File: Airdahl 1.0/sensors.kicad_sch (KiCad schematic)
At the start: 26 parts, among them J7 CONUFL001-SMD-T, J9 104031-0811, U4 BNO085, U5 BMP581, U6 RFM95W-915S2

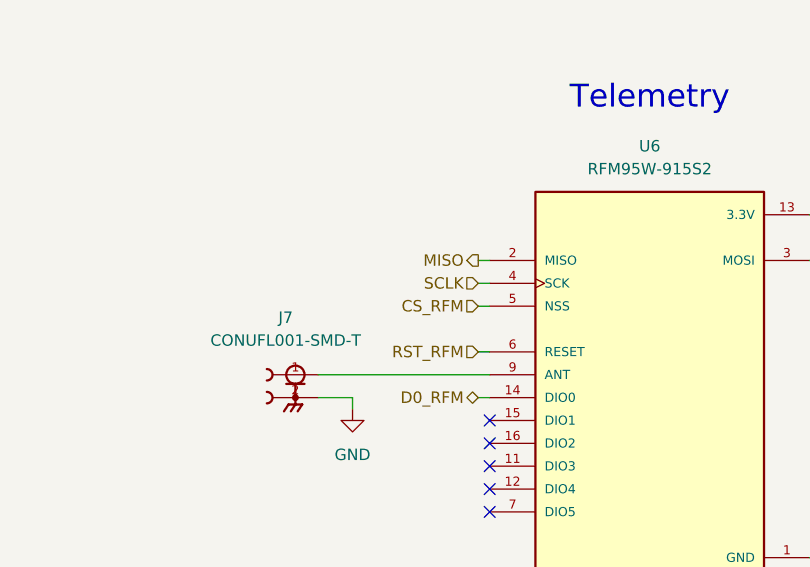
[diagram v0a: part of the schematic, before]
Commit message: H-Bridge wiring + motor ports, cleaned up carrier schematics, added MISO source terminating resistors on carriers
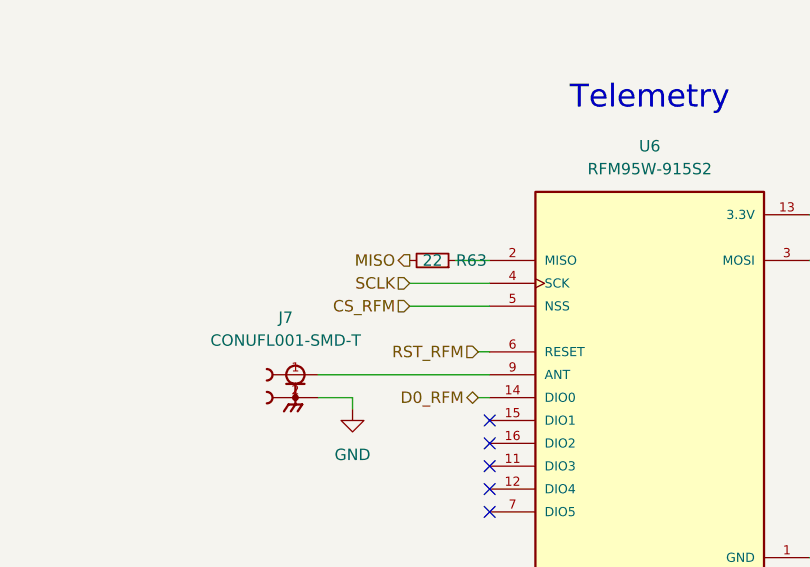
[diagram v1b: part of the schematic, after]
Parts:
- added R63: 22, Resistor_SMD:R_0402_1005Metric, symbol Device:R_Small
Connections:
- net MISO: now also R63.2; no longer U6.2 (MISO)
- new net: R63.1, U6.2 (MISO)
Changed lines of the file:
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@@
 	(wire
 		(pts
-			(xy 218.44 102.87) (xy 219.71 102.87)
+			(xy 210.82 102.87) (xy 219.71 102.87)
 		)
 		(stroke
@@
 	(wire
 		(pts
-			(xy 218.44 100.33) (xy 219.71 100.33)
+			(xy 210.82 100.33) (xy 219.71 100.33)
 		)
 		(stroke
@@
 	(wire
 		(pts
-			(xy 218.44 97.79) (xy 219.71 97.79)
-		)
-		(stroke
-			(width 0)
-			(type default)
-		)
-	)
-	(wire
-		(pts
 			(xy 52.07 146.05) (xy 48.26 146.05)
 		)
@@
 	(wire
 		(pts
+			(xy 215.9 97.79) (xy 219.71 97.79)
+		)
+		(stroke
+			(width 0)
+			(type default)
+		)
+	)
+	(wire
+		(pts
 			(xy 96.52 48.26) (xy 111.76 48.26)
 		)
@@
 	(hierarchical_label "SCLK"
 		(shape input)
-		(at 218.44 100.33 180)
+		(at 210.82 100.33 180)
 		(effects
 			(font
@@
 	(hierarchical_label "MISO"
 		(shape output)
-		(at 218.44 97.79 180)
+		(at 210.82 97.79 180)
 		(effects
 			(font
@@
 	(hierarchical_label "CS_RFM"
 		(shape input)
-		(at 218.44 102.87 180)
+		(at 210.82 102.87 180)
 		(effects
 			(font
@@
 					(unit 1)
 				)
+			)
+		)
+	)
+	(symbol
+		(lib_id "Device:R_Small")
+		(at 213.36 97.79 270)
+		(mirror x)
+		(unit 1)
+		(body_style 1)
+		(exclude_from_sim no)
+		(in_bom yes)
+		(on_board yes)
+		(in_pos_files yes)
+		(dnp no)
+		(property "Reference" "R63"
+			(at 217.678 97.79 90)
+			(show_name no)
+			(do_not_autoplace no)
+			(effects
+				(font
+					(size 1.27 1.27)
+				)
+			)
+		)
+		(property "Value" "22"
+			(at 213.36 97.79 90)
+			(show_name no)
+			(do_not_autoplace no)
+			(effects
+				(font
+					(size 1.27 1.27)
+				)
+			)
+		)
+		(property "Footprint" "Resistor_SMD:R_0402_1005Metric"
+			(at 213.36 97.79 0)
+			(hide yes)
+			(show_name no)
+			(do_not_autoplace no)
+			(effects
+				(font
+					(size 1.27 1.27)
+				)
+			)
+		)
+		(property "Datasheet" ""
+			(at 213.36 97.79 0)
+			(hide yes)
+			(show_name no)
+			(do_not_autoplace no)
+			(effects
+				(font
+					(size 1.27 1.27)
+				)
+			)
+		)
+		(property "Description" "Resistor, small symbol"
+			(at 213.36 97.79 0)
+			(hide yes)
+			(show_name no)
+			(do_not_autoplace no)
+			(effects
+				(font
+					(size 1.27 1.27)
+				)
+			)
+		)
+		(pin "2"
+		)
+		(pin "1"
+		)
+		(instances
+			(project "Airdahl 1.0"
+				(path "/e2c992a5-0f37-48ff-88a4-7c40cfcda45e/bd752d91-9d5e-4749-819a-1163586784de"
+					(reference "R63")
+					(unit 1)
+				)

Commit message: some updates, mostly comments after schematic review
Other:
- note added: "On RFM95W board, there isn't any impedance matching to antenna port. Double check that RFM95W to Pi/Arduino communication works"
- note added: "SDIO rather than SPI"
- note added: "double check SDIO pull-ups, including value."
- moved on the sheet: C17, J9, R52, R53, R54, R55, R56, R57
